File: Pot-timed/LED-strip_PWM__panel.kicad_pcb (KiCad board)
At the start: 2 copper layers, 160 x 100 mm, 76 parts, among them IC1 ATTINY13A-MM, P1 CONN_2, P2 CONN_2, T1 AO3400, U1 MCP1804-SOT23-5

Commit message: Pot-timed: Tweaked the panel (paste layer for stencil).
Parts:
- removed the 1PIN at (104.0, 97.0)
- removed the 1PIN at (256.0, 97.0)
- removed the 1PIN at (104.0, 92.0)
- added BH1: BH1, 1pin, F.Cu at (104.0, 97.0)
- added C1: 100nF, MADW__C0805, F.Cu at (198.4, 93.9)
- added C1: 100nF, MADW__C0805, F.Cu at (220.4, 93.9)
- added C1: 100nF, MADW__C0805, F.Cu at (220.4, 124.5)
- added C1: 100nF, MADW__C0805, F.Cu at (220.4, 155.2)
- added C1: 100nF, MADW__C0805, F.Cu at (209.4, 155.2)
- added C1: 100nF, MADW__C0805, F.Cu at (209.4, 124.5)
- added C1: 100nF, MADW__C0805, F.Cu at (209.4, 93.9)
- added C1: 100nF, MADW__C0805, F.Cu at (154.4, 93.9)
- added C1: 100nF, MADW__C0805, F.Cu at (154.4, 124.5)
- added C1: 100nF, MADW__C0805, F.Cu at (154.4, 155.2)
- added C1: 100nF, MADW__C0805, F.Cu at (165.4, 155.2)
- added C1: 100nF, MADW__C0805, F.Cu at (198.4, 124.5)
- added C1: 100nF, MADW__C0805, F.Cu at (165.4, 124.5)
- added C1: 100nF, MADW__C0805, F.Cu at (165.4, 93.9)
- added C1: 100nF, MADW__C0805, F.Cu at (187.4, 93.9)
- added C1: 100nF, MADW__C0805, F.Cu at (187.4, 124.5)
- added C1: 100nF, MADW__C0805, F.Cu at (187.4, 155.2)
- added C1: 100nF, MADW__C0805, F.Cu at (176.4, 155.2)
- added C1: 100nF, MADW__C0805, F.Cu at (176.4, 124.5)
- added C1: 100nF, MADW__C0805, F.Cu at (176.4, 93.9)
- added C1: 100nF, MADW__C0805, F.Cu at (132.4, 93.9)
- added C1: 100nF, MADW__C0805, F.Cu at (132.4, 124.5)
- added C1: 100nF, MADW__C0805, F.Cu at (198.4, 155.2)
- added C1: 100nF, MADW__C0805, F.Cu at (132.4, 155.2)
- added C1: 100nF, MADW__C0805, F.Cu at (143.4, 155.2)
- added C1: 100nF, MADW__C0805, F.Cu at (143.4, 124.5)
- added C1: 100nF, MADW__C0805, F.Cu at (143.4, 93.9)
- added C1: 100nF, MADW__C0805, F.Cu at (121.5, 93.9)
- added C1: 100nF, MADW__C0805, F.Cu at (121.5, 124.5)
- added C1: 100nF, MADW__C0805, F.Cu at (121.5, 155.2)
- added C1: 100nF, MADW__C0805, F.Cu at (231.4, 93.9)
- added C1: 100nF, MADW__C0805, F.Cu at (231.4, 124.5)
- added C1: 100nF, MADW__C0805, F.Cu at (231.4, 155.2)
- added C1: 100nF, MADW__C0805, F.Cu at (242.4, 155.2)
- added C1: 100nF, MADW__C0805, F.Cu at (242.4, 124.5)
- added C1: 100nF, MADW__C0805, F.Cu at (242.4, 93.9)
- added C2: 100nF, MADW__C0805, F.Cu at (204.4, 91.4)
- added C2: 100nF, MADW__C0805, F.Cu at (226.4, 91.4)
- added C2: 100nF, MADW__C0805, F.Cu at (226.4, 122.0)
- added C2: 100nF, MADW__C0805, F.Cu at (226.4, 152.7)
- added C2: 100nF, MADW__C0805, F.Cu at (215.4, 152.7)
- added C2: 100nF, MADW__C0805, F.Cu at (215.4, 122.0)
- added C2: 100nF, MADW__C0805, F.Cu at (215.4, 91.4)
- added C2: 100nF, MADW__C0805, F.Cu at (160.4, 91.4)
- added C2: 100nF, MADW__C0805, F.Cu at (160.4, 122.0)
- added C2: 100nF, MADW__C0805, F.Cu at (160.4, 152.7)
- added C2: 100nF, MADW__C0805, F.Cu at (171.4, 152.7)
- added C2: 100nF, MADW__C0805, F.Cu at (204.4, 122.0)
- added C2: 100nF, MADW__C0805, F.Cu at (171.4, 122.0)
- added C2: 100nF, MADW__C0805, F.Cu at (171.4, 91.4)
- added C2: 100nF, MADW__C0805, F.Cu at (193.4, 91.4)
- added C2: 100nF, MADW__C0805, F.Cu at (193.4, 122.0)
- added C2: 100nF, MADW__C0805, F.Cu at (193.4, 152.7)
- added C2: 100nF, MADW__C0805, F.Cu at (182.4, 152.7)
- added C2: 100nF, MADW__C0805, F.Cu at (182.4, 122.0)
- added C2: 100nF, MADW__C0805, F.Cu at (182.4, 91.4)
- added C2: 100nF, MADW__C0805, F.Cu at (138.4, 91.4)
- added C2: 100nF, MADW__C0805, F.Cu at (138.4, 122.0)
- added C2: 100nF, MADW__C0805, F.Cu at (204.4, 152.7)
- added C2: 100nF, MADW__C0805, F.Cu at (138.4, 152.7)
- added C2: 100nF, MADW__C0805, F.Cu at (149.4, 152.7)
- added C2: 100nF, MADW__C0805, F.Cu at (149.4, 122.0)
- added C2: 100nF, MADW__C0805, F.Cu at (149.4, 91.4)
- added C2: 100nF, MADW__C0805, F.Cu at (127.5, 91.4)
- added C2: 100nF, MADW__C0805, F.Cu at (127.5, 122.0)
- added C2: 100nF, MADW__C0805, F.Cu at (127.5, 152.7)
- added C2: 100nF, MADW__C0805, F.Cu at (237.4, 91.4)
- added C2: 100nF, MADW__C0805, F.Cu at (237.4, 122.0)
- added C2: 100nF, MADW__C0805, F.Cu at (237.4, 152.7)
- added C2: 100nF, MADW__C0805, F.Cu at (248.4, 152.7)
- added C2: 100nF, MADW__C0805, F.Cu at (248.4, 122.0)
- added C2: 100nF, MADW__C0805, F.Cu at (248.4, 91.4)
- added C3: 4.7µF, MADW__C0805, F.Cu at (200.9, 93.9)
- added C3: 4.7µF, MADW__C0805, F.Cu at (222.9, 93.9)
- added C3: 4.7µF, MADW__C0805, F.Cu at (222.9, 124.5)
- added C3: 4.7µF, MADW__C0805, F.Cu at (222.9, 155.2)
- added C3: 4.7µF, MADW__C0805, F.Cu at (211.9, 155.2)
- added C3: 4.7µF, MADW__C0805, F.Cu at (211.9, 124.5)
- added C3: 4.7µF, MADW__C0805, F.Cu at (211.9, 93.9)
- added C3: 4.7µF, MADW__C0805, F.Cu at (156.9, 93.9)
- added C3: 4.7µF, MADW__C0805, F.Cu at (156.9, 124.5)
- added C3: 4.7µF, MADW__C0805, F.Cu at (156.9, 155.2)
- added C3: 4.7µF, MADW__C0805, F.Cu at (167.9, 155.2)
- added C3: 4.7µF, MADW__C0805, F.Cu at (200.9, 124.5)
- added C3: 4.7µF, MADW__C0805, F.Cu at (167.9, 124.5)
- added C3: 4.7µF, MADW__C0805, F.Cu at (167.9, 93.9)
- added C3: 4.7µF, MADW__C0805, F.Cu at (189.9, 93.9)
- added C3: 4.7µF, MADW__C0805, F.Cu at (189.9, 124.5)
- added C3: 4.7µF, MADW__C0805, F.Cu at (189.9, 155.2)
- added C3: 4.7µF, MADW__C0805, F.Cu at (178.9, 155.2)
- added C3: 4.7µF, MADW__C0805, F.Cu at (178.9, 124.5)
- added C3: 4.7µF, MADW__C0805, F.Cu at (178.9, 93.9)
- added C3: 4.7µF, MADW__C0805, F.Cu at (134.9, 93.9)
- added C3: 4.7µF, MADW__C0805, F.Cu at (134.9, 124.5)
- added C3: 4.7µF, MADW__C0805, F.Cu at (200.9, 155.2)
- added C3: 4.7µF, MADW__C0805, F.Cu at (134.9, 155.2)
- added C3: 4.7µF, MADW__C0805, F.Cu at (145.9, 155.2)
- added C3: 4.7µF, MADW__C0805, F.Cu at (145.9, 124.5)
- added C3: 4.7µF, MADW__C0805, F.Cu at (145.9, 93.9)
- added C3: 4.7µF, MADW__C0805, F.Cu at (124.0, 93.9)
- added C3: 4.7µF, MADW__C0805, F.Cu at (124.0, 124.5)
- added C3: 4.7µF, MADW__C0805, F.Cu at (124.0, 155.2)
- added C3: 4.7µF, MADW__C0805, F.Cu at (233.9, 93.9)
- added C3: 4.7µF, MADW__C0805, F.Cu at (233.9, 124.5)
- added C3: 4.7µF, MADW__C0805, F.Cu at (233.9, 155.2)
- added C3: 4.7µF, MADW__C0805, F.Cu at (244.9, 155.2)
- added C3: 4.7µF, MADW__C0805, F.Cu at (244.9, 124.5)
- added C3: 4.7µF, MADW__C0805, F.Cu at (244.9, 93.9)
- added G1: OSHW-logo_silkscreen_3mm, OSHW-logo_silkscreen_3mm, B.Cu at (201.2, 105.5)
- added G1: OSHW-logo_silkscreen_3mm, OSHW-logo_silkscreen_3mm, B.Cu at (223.2, 105.5)
- added G1: OSHW-logo_silkscreen_3mm, OSHW-logo_silkscreen_3mm, B.Cu at (223.2, 136.1)
- added G1: OSHW-logo_silkscreen_3mm, OSHW-logo_silkscreen_3mm, B.Cu at (223.2, 166.8)
- added G1: OSHW-logo_silkscreen_3mm, OSHW-logo_silkscreen_3mm, B.Cu at (212.2, 166.8)
- added G1: OSHW-logo_silkscreen_3mm, OSHW-logo_silkscreen_3mm, B.Cu at (212.2, 136.1)
- added G1: OSHW-logo_silkscreen_3mm, OSHW-logo_silkscreen_3mm, B.Cu at (212.2, 105.5)
- added G1: OSHW-logo_silkscreen_3mm, OSHW-logo_silkscreen_3mm, B.Cu at (157.2, 105.5)
- added G1: OSHW-logo_silkscreen_3mm, OSHW-logo_silkscreen_3mm, B.Cu at (157.2, 136.1)
- added G1: OSHW-logo_silkscreen_3mm, OSHW-logo_silkscreen_3mm, B.Cu at (157.2, 166.8)
- added G1: OSHW-logo_silkscreen_3mm, OSHW-logo_silkscreen_3mm, B.Cu at (168.2, 166.8)
- added G1: OSHW-logo_silkscreen_3mm, OSHW-logo_silkscreen_3mm, B.Cu at (201.2, 136.1)
- added G1: OSHW-logo_silkscreen_3mm, OSHW-logo_silkscreen_3mm, B.Cu at (168.2, 136.1)
- added G1: OSHW-logo_silkscreen_3mm, OSHW-logo_silkscreen_3mm, B.Cu at (168.2, 105.5)
- added G1: OSHW-logo_silkscreen_3mm, OSHW-logo_silkscreen_3mm, B.Cu at (190.2, 105.5)
- added G1: OSHW-logo_silkscreen_3mm, OSHW-logo_silkscreen_3mm, B.Cu at (190.2, 136.1)
- added G1: OSHW-logo_silkscreen_3mm, OSHW-logo_silkscreen_3mm, B.Cu at (190.2, 166.8)
- added G1: OSHW-logo_silkscreen_3mm, OSHW-logo_silkscreen_3mm, B.Cu at (179.2, 166.8)
- added G1: OSHW-logo_silkscreen_3mm, OSHW-logo_silkscreen_3mm, B.Cu at (179.2, 136.1)
- added G1: OSHW-logo_silkscreen_3mm, OSHW-logo_silkscreen_3mm, B.Cu at (179.2, 105.5)
- added G1: OSHW-logo_silkscreen_3mm, OSHW-logo_silkscreen_3mm, B.Cu at (135.2, 105.5)
- added G1: OSHW-logo_silkscreen_3mm, OSHW-logo_silkscreen_3mm, B.Cu at (135.2, 136.1)
- added G1: OSHW-logo_silkscreen_3mm, OSHW-logo_silkscreen_3mm, B.Cu at (201.2, 166.8)
- added G1: OSHW-logo_silkscreen_3mm, OSHW-logo_silkscreen_3mm, B.Cu at (135.2, 166.8)
- added G1: OSHW-logo_silkscreen_3mm, OSHW-logo_silkscreen_3mm, B.Cu at (146.2, 166.8)
- added G1: OSHW-logo_silkscreen_3mm, OSHW-logo_silkscreen_3mm, B.Cu at (146.2, 136.1)
- added G1: OSHW-logo_silkscreen_3mm, OSHW-logo_silkscreen_3mm, B.Cu at (146.2, 105.5)
- added G1: OSHW-logo_silkscreen_3mm, OSHW-logo_silkscreen_3mm, B.Cu at (124.2, 105.5)
- added G1: OSHW-logo_silkscreen_3mm, OSHW-logo_silkscreen_3mm, B.Cu at (124.2, 136.1)
- added G1: OSHW-logo_silkscreen_3mm, OSHW-logo_silkscreen_3mm, B.Cu at (124.2, 166.8)
- added G1: OSHW-logo_silkscreen_3mm, OSHW-logo_silkscreen_3mm, B.Cu at (234.2, 105.5)
- added G1: OSHW-logo_silkscreen_3mm, OSHW-logo_silkscreen_3mm, B.Cu at (234.2, 136.1)
- added G1: OSHW-logo_silkscreen_3mm, OSHW-logo_silkscreen_3mm, B.Cu at (234.2, 166.8)
- added G1: OSHW-logo_silkscreen_3mm, OSHW-logo_silkscreen_3mm, B.Cu at (245.2, 166.8)
- added G1: OSHW-logo_silkscreen_3mm, OSHW-logo_silkscreen_3mm, B.Cu at (245.2, 136.1)
- added G1: OSHW-logo_silkscreen_3mm, OSHW-logo_silkscreen_3mm, B.Cu at (245.2, 105.5)
- added G2: LED_smile_silkscreen_3mm, LED_smile_silkscreen_3mm, B.Cu at (201.2, 93.4)
- added G2: LED_smile_silkscreen_3mm, LED_smile_silkscreen_3mm, B.Cu at (223.2, 93.4)
- added G2: LED_smile_silkscreen_3mm, LED_smile_silkscreen_3mm, B.Cu at (223.2, 124.1)
- added G2: LED_smile_silkscreen_3mm, LED_smile_silkscreen_3mm, B.Cu at (223.2, 154.7)
- added G2: LED_smile_silkscreen_3mm, LED_smile_silkscreen_3mm, B.Cu at (212.2, 154.7)
- added G2: LED_smile_silkscreen_3mm, LED_smile_silkscreen_3mm, B.Cu at (212.2, 124.1)
- added G2: LED_smile_silkscreen_3mm, LED_smile_silkscreen_3mm, B.Cu at (212.2, 93.4)
- added G2: LED_smile_silkscreen_3mm, LED_smile_silkscreen_3mm, B.Cu at (157.2, 93.4)
- added G2: LED_smile_silkscreen_3mm, LED_smile_silkscreen_3mm, B.Cu at (157.2, 124.1)
- added G2: LED_smile_silkscreen_3mm, LED_smile_silkscreen_3mm, B.Cu at (157.2, 154.7)
- added G2: LED_smile_silkscreen_3mm, LED_smile_silkscreen_3mm, B.Cu at (168.2, 154.7)
- added G2: LED_smile_silkscreen_3mm, LED_smile_silkscreen_3mm, B.Cu at (201.2, 124.1)
- added G2: LED_smile_silkscreen_3mm, LED_smile_silkscreen_3mm, B.Cu at (168.2, 124.1)
- added G2: LED_smile_silkscreen_3mm, LED_smile_silkscreen_3mm, B.Cu at (168.2, 93.4)
- added G2: LED_smile_silkscreen_3mm, LED_smile_silkscreen_3mm, B.Cu at (190.2, 93.4)
- added G2: LED_smile_silkscreen_3mm, LED_smile_silkscreen_3mm, B.Cu at (190.2, 124.1)
- added G2: LED_smile_silkscreen_3mm, LED_smile_silkscreen_3mm, B.Cu at (190.2, 154.7)
- added G2: LED_smile_silkscreen_3mm, LED_smile_silkscreen_3mm, B.Cu at (179.2, 154.7)
- added G2: LED_smile_silkscreen_3mm, LED_smile_silkscreen_3mm, B.Cu at (179.2, 124.1)
- added G2: LED_smile_silkscreen_3mm, LED_smile_silkscreen_3mm, B.Cu at (179.2, 93.4)
- added G2: LED_smile_silkscreen_3mm, LED_smile_silkscreen_3mm, B.Cu at (135.2, 93.4)
- added G2: LED_smile_silkscreen_3mm, LED_smile_silkscreen_3mm, B.Cu at (135.2, 124.1)
- added G2: LED_smile_silkscreen_3mm, LED_smile_silkscreen_3mm, B.Cu at (201.2, 154.7)
- added G2: LED_smile_silkscreen_3mm, LED_smile_silkscreen_3mm, B.Cu at (135.2, 154.7)
- added G2: LED_smile_silkscreen_3mm, LED_smile_silkscreen_3mm, B.Cu at (146.2, 154.7)
- added G2: LED_smile_silkscreen_3mm, LED_smile_silkscreen_3mm, B.Cu at (146.2, 124.1)
- added G2: LED_smile_silkscreen_3mm, LED_smile_silkscreen_3mm, B.Cu at (146.2, 93.4)
- added G2: LED_smile_silkscreen_3mm, LED_smile_silkscreen_3mm, B.Cu at (124.2, 93.4)
- added G2: LED_smile_silkscreen_3mm, LED_smile_silkscreen_3mm, B.Cu at (124.2, 124.1)
- added G2: LED_smile_silkscreen_3mm, LED_smile_silkscreen_3mm, B.Cu at (124.2, 154.7)
- added G2: LED_smile_silkscreen_3mm, LED_smile_silkscreen_3mm, B.Cu at (234.2, 93.4)
- added G2: LED_smile_silkscreen_3mm, LED_smile_silkscreen_3mm, B.Cu at (234.2, 124.1)
- added G2: LED_smile_silkscreen_3mm, LED_smile_silkscreen_3mm, B.Cu at (234.2, 154.7)
- added G2: LED_smile_silkscreen_3mm, LED_smile_silkscreen_3mm, B.Cu at (245.2, 154.7)
- added G2: LED_smile_silkscreen_3mm, LED_smile_silkscreen_3mm, B.Cu at (245.2, 124.1)
- added G2: LED_smile_silkscreen_3mm, LED_smile_silkscreen_3mm, B.Cu at (245.2, 93.4)
- added IC1: ATTINY13A-MM, MADW__MLF10, F.Cu at (204.2, 99.2)
- added IC1: ATTINY13A-MM, MADW__MLF10, F.Cu at (226.2, 99.2)
- added IC1: ATTINY13A-MM, MADW__MLF10, F.Cu at (226.2, 129.9)
- added IC1: ATTINY13A-MM, MADW__MLF10, F.Cu at (226.2, 160.5)
- added IC1: ATTINY13A-MM, MADW__MLF10, F.Cu at (215.2, 160.5)
- added IC1: ATTINY13A-MM, MADW__MLF10, F.Cu at (215.2, 129.9)
- added IC1: ATTINY13A-MM, MADW__MLF10, F.Cu at (215.2, 99.2)
- added IC1: ATTINY13A-MM, MADW__MLF10, F.Cu at (160.2, 99.2)
- added IC1: ATTINY13A-MM, MADW__MLF10, F.Cu at (160.2, 129.9)
- added IC1: ATTINY13A-MM, MADW__MLF10, F.Cu at (160.2, 160.5)
- added IC1: ATTINY13A-MM, MADW__MLF10, F.Cu at (171.2, 160.5)
- added IC1: ATTINY13A-MM, MADW__MLF10, F.Cu at (204.2, 129.9)
- added IC1: ATTINY13A-MM, MADW__MLF10, F.Cu at (171.2, 129.9)
- added IC1: ATTINY13A-MM, MADW__MLF10, F.Cu at (171.2, 99.2)
- added IC1: ATTINY13A-MM, MADW__MLF10, F.Cu at (193.2, 99.2)
- added IC1: ATTINY13A-MM, MADW__MLF10, F.Cu at (193.2, 129.9)
- added IC1: ATTINY13A-MM, MADW__MLF10, F.Cu at (193.2, 160.5)
- added IC1: ATTINY13A-MM, MADW__MLF10, F.Cu at (182.2, 160.5)
- added IC1: ATTINY13A-MM, MADW__MLF10, F.Cu at (182.2, 129.9)
- added IC1: ATTINY13A-MM, MADW__MLF10, F.Cu at (182.2, 99.2)
- added IC1: ATTINY13A-MM, MADW__MLF10, F.Cu at (138.2, 99.2)
- added IC1: ATTINY13A-MM, MADW__MLF10, F.Cu at (138.2, 129.9)
- added IC1: ATTINY13A-MM, MADW__MLF10, F.Cu at (204.2, 160.5)
- added IC1: ATTINY13A-MM, MADW__MLF10, F.Cu at (138.2, 160.5)
- added IC1: ATTINY13A-MM, MADW__MLF10, F.Cu at (149.2, 160.5)
- added IC1: ATTINY13A-MM, MADW__MLF10, F.Cu at (149.2, 129.9)
- added IC1: ATTINY13A-MM, MADW__MLF10, F.Cu at (149.2, 99.2)
- added IC1: ATTINY13A-MM, MADW__MLF10, F.Cu at (127.2, 99.2)
- added IC1: ATTINY13A-MM, MADW__MLF10, F.Cu at (127.2, 129.9)
- added IC1: ATTINY13A-MM, MADW__MLF10, F.Cu at (127.2, 160.5)
- added IC1: ATTINY13A-MM, MADW__MLF10, F.Cu at (237.2, 99.2)
- added IC1: ATTINY13A-MM, MADW__MLF10, F.Cu at (237.2, 129.9)
- added IC1: ATTINY13A-MM, MADW__MLF10, F.Cu at (237.2, 160.5)
- added IC1: ATTINY13A-MM, MADW__MLF10, F.Cu at (248.2, 160.5)
- added IC1: ATTINY13A-MM, MADW__MLF10, F.Cu at (248.2, 129.9)
- added IC1: ATTINY13A-MM, MADW__MLF10, F.Cu at (248.2, 99.2)
- added JP1: ISP, MADW__PIN_ARRAY_3x2_1.27mm, F.Cu at (199.7, 99.2)
- added JP1: ISP, MADW__PIN_ARRAY_3x2_1.27mm, F.Cu at (221.7, 99.2)
- added JP1: ISP, MADW__PIN_ARRAY_3x2_1.27mm, F.Cu at (221.7, 129.9)
- added JP1: ISP, MADW__PIN_ARRAY_3x2_1.27mm, F.Cu at (221.7, 160.5)
- added JP1: ISP, MADW__PIN_ARRAY_3x2_1.27mm, F.Cu at (210.7, 160.5)
- added JP1: ISP, MADW__PIN_ARRAY_3x2_1.27mm, F.Cu at (210.7, 129.9)
- added JP1: ISP, MADW__PIN_ARRAY_3x2_1.27mm, F.Cu at (210.7, 99.2)
- added JP1: ISP, MADW__PIN_ARRAY_3x2_1.27mm, F.Cu at (155.7, 99.2)
- added JP1: ISP, MADW__PIN_ARRAY_3x2_1.27mm, F.Cu at (155.7, 129.9)
- added JP1: ISP, MADW__PIN_ARRAY_3x2_1.27mm, F.Cu at (155.7, 160.5)
- added JP1: ISP, MADW__PIN_ARRAY_3x2_1.27mm, F.Cu at (166.7, 160.5)
- added JP1: ISP, MADW__PIN_ARRAY_3x2_1.27mm, F.Cu at (199.7, 129.9)
- added JP1: ISP, MADW__PIN_ARRAY_3x2_1.27mm, F.Cu at (166.7, 129.9)
- added JP1: ISP, MADW__PIN_ARRAY_3x2_1.27mm, F.Cu at (166.7, 99.2)
- added JP1: ISP, MADW__PIN_ARRAY_3x2_1.27mm, F.Cu at (188.7, 99.2)
- added JP1: ISP, MADW__PIN_ARRAY_3x2_1.27mm, F.Cu at (188.7, 129.9)
- added JP1: ISP, MADW__PIN_ARRAY_3x2_1.27mm, F.Cu at (188.7, 160.5)
- added JP1: ISP, MADW__PIN_ARRAY_3x2_1.27mm, F.Cu at (177.7, 160.5)
- added JP1: ISP, MADW__PIN_ARRAY_3x2_1.27mm, F.Cu at (177.7, 129.9)
- added JP1: ISP, MADW__PIN_ARRAY_3x2_1.27mm, F.Cu at (177.7, 99.2)
- added JP1: ISP, MADW__PIN_ARRAY_3x2_1.27mm, F.Cu at (133.7, 99.2)
- added JP1: ISP, MADW__PIN_ARRAY_3x2_1.27mm, F.Cu at (133.7, 129.9)
- added JP1: ISP, MADW__PIN_ARRAY_3x2_1.27mm, F.Cu at (199.7, 160.5)
- added JP1: ISP, MADW__PIN_ARRAY_3x2_1.27mm, F.Cu at (133.7, 160.5)
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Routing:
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
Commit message: Pot-timed: Panel partially updated.
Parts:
- removed the C1 at (198.4, 93.9)
- removed the C1 at (220.4, 93.9)
- removed the C1 at (220.4, 124.5)
- removed the C1 at (220.4, 155.2)
- removed the C1 at (209.4, 155.2)
- removed the C1 at (209.4, 124.5)
- removed the C1 at (209.4, 93.9)
- removed the C1 at (154.4, 93.9)
- removed the C1 at (154.4, 124.5)
- removed the C1 at (154.4, 155.2)
- removed the C1 at (165.4, 155.2)
- removed the C1 at (198.4, 124.5)
- removed the C1 at (165.4, 124.5)
- removed the C1 at (165.4, 93.9)
- removed the C1 at (187.4, 93.9)
- removed the C1 at (187.4, 124.5)
- removed the C1 at (187.4, 155.2)
- removed the C1 at (176.4, 155.2)
- removed the C1 at (176.4, 124.5)
- removed the C1 at (176.4, 93.9)
- removed the C1 at (132.4, 93.9)
- removed the C1 at (132.4, 124.5)
- removed the C1 at (198.4, 155.2)
- removed the C1 at (132.4, 155.2)
- removed the C1 at (143.4, 155.2)
- removed the C1 at (143.4, 124.5)
- removed the C1 at (143.4, 93.9)
- removed the C1 at (121.5, 93.9)
- removed the C1 at (121.5, 124.5)
- removed the C1 at (121.5, 155.2)
- removed the C1 at (231.4, 93.9)
- removed the C1 at (231.4, 124.5)
- removed the C1 at (231.4, 155.2)
- removed the C1 at (242.4, 155.2)
- removed the C1 at (242.4, 124.5)
- removed the C1 at (242.4, 93.9)
- removed the C2 at (204.4, 91.4)
- removed the C2 at (226.4, 91.4)
- removed the C2 at (226.4, 122.0)
- removed the C2 at (226.4, 152.7)
- removed the C2 at (215.4, 152.7)
- removed the C2 at (215.4, 122.0)
- removed the C2 at (215.4, 91.4)
- removed the C2 at (160.4, 91.4)
- removed the C2 at (160.4, 122.0)
- removed the C2 at (160.4, 152.7)
- removed the C2 at (171.4, 152.7)
- removed the C2 at (204.4, 122.0)
- removed the C2 at (171.4, 122.0)
- removed the C2 at (171.4, 91.4)
- removed the C2 at (193.4, 91.4)
- removed the C2 at (193.4, 122.0)
- removed the C2 at (193.4, 152.7)
- removed the C2 at (182.4, 152.7)
- removed the C2 at (182.4, 122.0)
- removed the C2 at (182.4, 91.4)
- removed the C2 at (138.4, 91.4)
- removed the C2 at (138.4, 122.0)
- removed the C2 at (204.4, 152.7)
- removed the C2 at (138.4, 152.7)
- removed the C2 at (149.4, 152.7)
- removed the C2 at (149.4, 122.0)
- removed the C2 at (149.4, 91.4)
- removed the C2 at (127.5, 91.4)
- removed the C2 at (127.5, 122.0)
- removed the C2 at (127.5, 152.7)
- removed the C2 at (237.4, 91.4)
- removed the C2 at (237.4, 122.0)
- removed the C2 at (237.4, 152.7)
- removed the C2 at (248.4, 152.7)
- removed the C2 at (248.4, 122.0)
- removed the C2 at (248.4, 91.4)
- removed the C3 at (200.9, 93.9)
- removed the C3 at (222.9, 93.9)
- removed the C3 at (222.9, 124.5)
- removed the C3 at (222.9, 155.2)
- removed the C3 at (211.9, 155.2)
- removed the C3 at (211.9, 124.5)
- removed the C3 at (211.9, 93.9)
- removed the C3 at (156.9, 93.9)
- removed the C3 at (156.9, 124.5)
- removed the C3 at (156.9, 155.2)
- removed the C3 at (167.9, 155.2)
- removed the C3 at (200.9, 124.5)
- removed the C3 at (167.9, 124.5)
- removed the C3 at (167.9, 93.9)
- removed the C3 at (189.9, 93.9)
- removed the C3 at (189.9, 124.5)
- removed the C3 at (189.9, 155.2)
- removed the C3 at (178.9, 155.2)
- removed the C3 at (178.9, 124.5)
- removed the C3 at (178.9, 93.9)
- removed the C3 at (134.9, 93.9)
- removed the C3 at (134.9, 124.5)
- removed the C3 at (200.9, 155.2)
- removed the C3 at (134.9, 155.2)
- removed the C3 at (145.9, 155.2)
- removed the C3 at (145.9, 124.5)
- removed the C3 at (145.9, 93.9)
- removed the C3 at (124.0, 93.9)
- removed the C3 at (124.0, 124.5)
- removed the C3 at (124.0, 155.2)
- removed the C3 at (233.9, 93.9)
- removed the C3 at (233.9, 124.5)
- removed the C3 at (233.9, 155.2)
- removed the C3 at (244.9, 155.2)
- removed the C3 at (244.9, 124.5)
- removed the C3 at (244.9, 93.9)
- removed the G1 at (201.2, 105.5)
- removed the G1 at (223.2, 105.5)
- removed the G1 at (223.2, 136.1)
- removed the G1 at (223.2, 166.8)
- removed the G1 at (212.2, 166.8)
- removed the G1 at (212.2, 136.1)
- removed the G1 at (212.2, 105.5)
- removed the G1 at (157.2, 105.5)
- removed the G1 at (157.2, 136.1)
- removed the G1 at (157.2, 166.8)
- removed the G1 at (168.2, 166.8)
- removed the G1 at (201.2, 136.1)
- removed the G1 at (168.2, 136.1)
- removed the G1 at (168.2, 105.5)
- removed the G1 at (190.2, 105.5)
- removed the G1 at (190.2, 136.1)
- removed the G1 at (190.2, 166.8)
- removed the G1 at (179.2, 166.8)
- removed the G1 at (179.2, 136.1)
- removed the G1 at (179.2, 105.5)
- removed the G1 at (135.2, 105.5)
- removed the G1 at (135.2, 136.1)
- removed the G1 at (201.2, 166.8)
- removed the G1 at (135.2, 166.8)
- removed the G1 at (146.2, 166.8)
- removed the G1 at (146.2, 136.1)
- removed the G1 at (146.2, 105.5)
- removed the G1 at (124.2, 105.5)
- removed the G1 at (124.2, 136.1)
- removed the G1 at (124.2, 166.8)
- removed the G1 at (113.2, 166.8)
- removed the G1 at (113.2, 136.1)
- removed the G1 at (113.2, 105.5)
- removed the G1 at (234.2, 105.5)
- removed the G1 at (234.2, 136.1)
- removed the G1 at (234.2, 166.8)
- removed the G1 at (245.2, 166.8)
- removed the G1 at (245.2, 136.1)
- removed the G1 at (245.2, 105.5)
- removed the G2 at (201.2, 93.4)
- removed the G2 at (223.2, 93.4)
- removed the G2 at (223.2, 124.1)
- removed the G2 at (223.2, 154.7)
- removed the G2 at (212.2, 154.7)
- removed the G2 at (212.2, 124.1)
- removed the G2 at (212.2, 93.4)
- removed the G2 at (157.2, 93.4)
- removed the G2 at (157.2, 124.1)
- removed the G2 at (157.2, 154.7)
- removed the G2 at (168.2, 154.7)
- removed the G2 at (201.2, 124.1)
- removed the G2 at (168.2, 124.1)
- removed the G2 at (168.2, 93.4)
- removed the G2 at (190.2, 93.4)
- removed the G2 at (190.2, 124.1)
- removed the G2 at (190.2, 154.7)
- removed the G2 at (179.2, 154.7)
- removed the G2 at (179.2, 124.1)
- removed the G2 at (179.2, 93.4)
- removed the G2 at (135.2, 93.4)
- removed the G2 at (135.2, 124.1)
- removed the G2 at (201.2, 154.7)
- removed the G2 at (135.2, 154.7)
- removed the G2 at (146.2, 154.7)
- removed the G2 at (146.2, 124.1)
- removed the G2 at (146.2, 93.4)
- removed the G2 at (124.2, 93.4)
- removed the G2 at (124.2, 124.1)
- removed the G2 at (124.2, 154.7)
- removed the G2 at (113.2, 154.7)
- removed the G2 at (113.2, 124.1)
- removed the G2 at (113.2, 93.4)
- removed the G2 at (234.2, 93.4)
- removed the G2 at (234.2, 124.1)
- removed the G2 at (234.2, 154.7)
- removed the G2 at (245.2, 154.7)
- removed the G2 at (245.2, 124.1)
- removed the G2 at (245.2, 93.4)
- removed the IC1 at (204.2, 99.2)
- removed the IC1 at (226.2, 99.2)
- removed the IC1 at (226.2, 129.9)
- removed the IC1 at (226.2, 160.5)
- removed the IC1 at (215.2, 160.5)
- removed the IC1 at (215.2, 129.9)
- removed the IC1 at (215.2, 99.2)
- removed the IC1 at (160.2, 99.2)
- removed the IC1 at (160.2, 129.9)
- removed the IC1 at (160.2, 160.5)
- removed the IC1 at (171.2, 160.5)
- removed the IC1 at (204.2, 129.9)
- removed the IC1 at (171.2, 129.9)
- removed the IC1 at (171.2, 99.2)
- removed the IC1 at (193.2, 99.2)
- removed the IC1 at (193.2, 129.9)
- removed the IC1 at (193.2, 160.5)
- removed the IC1 at (182.2, 160.5)
- removed the IC1 at (182.2, 129.9)
- removed the IC1 at (182.2, 99.2)
- removed the IC1 at (138.2, 99.2)
- removed the IC1 at (138.2, 129.9)
- removed the IC1 at (204.2, 160.5)
- removed the IC1 at (138.2, 160.5)
- removed the IC1 at (149.2, 160.5)
- removed the IC1 at (149.2, 129.9)
- removed the IC1 at (149.2, 99.2)
- removed the IC1 at (127.2, 99.2)
- removed the IC1 at (127.2, 129.9)
- removed the IC1 at (127.2, 160.5)
- removed the IC1 at (237.2, 99.2)
- removed the IC1 at (237.2, 129.9)
- removed the IC1 at (237.2, 160.5)
- removed the IC1 at (248.2, 160.5)
- removed the IC1 at (248.2, 129.9)
- removed the IC1 at (248.2, 99.2)
- removed the JP1 at (199.7, 99.2)
- removed the JP1 at (221.7, 99.2)
- removed the JP1 at (221.7, 129.9)
- removed the JP1 at (221.7, 160.5)
- removed the JP1 at (210.7, 160.5)
- removed the JP1 at (210.7, 129.9)
- removed the JP1 at (210.7, 99.2)
- removed the JP1 at (155.7, 99.2)
- removed the JP1 at (155.7, 129.9)
- removed the JP1 at (155.7, 160.5)
- removed the JP1 at (166.7, 160.5)
- removed the JP1 at (199.7, 129.9)
- removed the JP1 at (166.7, 129.9)
- removed the JP1 at (166.7, 99.2)
- removed the JP1 at (188.7, 99.2)
- removed the JP1 at (188.7, 129.9)
- removed the JP1 at (188.7, 160.5)
- removed the JP1 at (177.7, 160.5)
- removed the JP1 at (177.7, 129.9)
- removed the JP1 at (177.7, 99.2)
- removed the JP1 at (133.7, 99.2)
- removed the JP1 at (133.7, 129.9)
- removed the JP1 at (199.7, 160.5)
- removed the JP1 at (133.7, 160.5)
- removed the JP1 at (144.7, 160.5)
- removed the JP1 at (144.7, 129.9)
- removed the JP1 at (144.7, 99.2)
- removed the JP1 at (122.7, 99.2)
- removed the JP1 at (122.7, 129.9)
- removed the JP1 at (122.7, 160.5)
- removed the JP1 at (232.7, 99.2)
- removed the JP1 at (232.7, 129.9)
- removed the JP1 at (232.7, 160.5)
- removed the JP1 at (243.7, 160.5)
- removed the JP1 at (243.7, 129.9)
- removed the JP1 at (243.7, 99.2)
- removed the NJ1 at (200.9, 90.8)
- removed the NJ1 at (222.9, 90.8)
- removed the NJ1 at (222.9, 121.5)
- removed the NJ1 at (222.9, 152.1)
- removed the NJ1 at (211.9, 152.1)
- removed the NJ1 at (211.9, 121.5)
- removed the NJ1 at (211.9, 90.8)
- removed the NJ1 at (156.9, 90.8)
- removed the NJ1 at (156.9, 121.5)
- removed the NJ1 at (156.9, 152.1)
- removed the NJ1 at (167.9, 152.1)
- removed the NJ1 at (200.9, 121.5)
- removed the NJ1 at (167.9, 121.5)
- removed the NJ1 at (167.9, 90.8)
- removed the NJ1 at (189.9, 90.8)
- removed the NJ1 at (189.9, 121.5)
- removed the NJ1 at (189.9, 152.1)
- removed the NJ1 at (178.9, 152.1)
- removed the NJ1 at (178.9, 121.5)
- removed the NJ1 at (178.9, 90.8)
- removed the NJ1 at (134.9, 90.8)
- removed the NJ1 at (134.9, 121.5)
- removed the NJ1 at (200.9, 152.1)
- removed the NJ1 at (134.9, 152.1)
- removed the NJ1 at (145.9, 152.1)
- removed the NJ1 at (145.9, 121.5)
- removed the NJ1 at (145.9, 90.8)
- removed the NJ1 at (124.0, 90.8)
- removed the NJ1 at (124.0, 121.5)
- removed the NJ1 at (124.0, 152.1)
- removed the NJ1 at (233.9, 90.8)
- removed the NJ1 at (233.9, 121.5)
- removed the NJ1 at (233.9, 152.1)
- removed the NJ1 at (244.9, 152.1)
- removed the NJ1 at (244.9, 121.5)
- removed the NJ1 at (244.9, 90.8)
- removed the P1 at (202.0, 88.3)
- removed the P1 at (224.0, 88.3)
- removed the P1 at (224.0, 118.9)
- removed the P1 at (224.0, 149.6)
- removed the P1 at (213.0, 149.6)
- removed the P1 at (213.0, 118.9)
- removed the P1 at (213.0, 88.3)
- removed the P1 at (158.0, 88.3)
- removed the P1 at (158.0, 118.9)
- removed the P1 at (158.0, 149.6)
- removed the P1 at (169.0, 149.6)
- removed the P1 at (202.0, 118.9)
- removed the P1 at (169.0, 118.9)
- removed the P1 at (169.0, 88.3)
- removed the P1 at (191.0, 88.3)
- removed the P1 at (191.0, 118.9)
- removed the P1 at (191.0, 149.6)
- removed the P1 at (180.0, 149.6)
- removed the P1 at (180.0, 118.9)
- removed the P1 at (180.0, 88.3)
- removed the P1 at (136.0, 88.3)
- removed the P1 at (136.0, 118.9)
- removed the P1 at (202.0, 149.6)
- removed the P1 at (136.0, 149.6)
- removed the P1 at (147.0, 149.6)
- removed the P1 at (147.0, 118.9)
- removed the P1 at (147.0, 88.3)
- removed the P1 at (125.0, 88.3)
- removed the P1 at (125.0, 118.9)
- removed the P1 at (125.0, 149.6)
- removed the P1 at (235.0, 88.3)
- removed the P1 at (235.0, 118.9)
- removed the P1 at (235.0, 149.6)
- removed the P1 at (246.0, 149.6)
- removed the P1 at (246.0, 118.9)
- removed the P1 at (246.0, 88.3)
- removed the P2 at (202.0, 114.5)
- removed the P2 at (224.0, 114.5)
- removed the P2 at (224.0, 145.1)
- removed the P2 at (224.0, 175.8)
- removed the P2 at (213.0, 175.8)
- removed the P2 at (213.0, 145.1)
- removed the P2 at (213.0, 114.5)
- removed the P2 at (158.0, 114.5)
- removed the P2 at (158.0, 145.1)
- removed the P2 at (158.0, 175.8)
- removed the P2 at (169.0, 175.8)
- removed the P2 at (202.0, 145.1)
- removed the P2 at (169.0, 145.1)
- removed the P2 at (169.0, 114.5)
- removed the P2 at (191.0, 114.5)
- removed the P2 at (191.0, 145.1)
- removed the P2 at (191.0, 175.8)
- removed the P2 at (180.0, 175.8)
- removed the P2 at (180.0, 145.1)
- removed the P2 at (180.0, 114.5)
- removed the P2 at (136.0, 114.5)
- removed the P2 at (136.0, 145.1)
- removed the P2 at (202.0, 175.8)
- removed the P2 at (136.0, 175.8)
- removed the P2 at (147.0, 175.8)
- removed the P2 at (147.0, 145.1)
- removed the P2 at (147.0, 114.5)
- removed the P2 at (125.0, 114.5)
- removed the P2 at (125.0, 145.1)
- removed the P2 at (125.0, 175.8)
- removed the P2 at (235.0, 114.5)
- removed the P2 at (235.0, 145.1)
- removed the P2 at (235.0, 175.8)
- removed the P2 at (246.0, 175.8)
- removed the P2 at (246.0, 145.1)
- removed the P2 at (246.0, 114.5)
- removed the R1 at (198.8, 110.4)
- removed the R1 at (220.8, 110.4)
- removed the R1 at (220.8, 141.0)
- removed the R1 at (220.8, 171.7)
- removed the R1 at (209.8, 171.7)
- removed the R1 at (209.8, 141.0)
- removed the R1 at (209.8, 110.4)
- removed the R1 at (154.8, 110.4)
- removed the R1 at (154.8, 141.0)
- removed the R1 at (154.8, 171.7)
- removed the R1 at (165.8, 171.7)
- removed the R1 at (198.8, 141.0)
- removed the R1 at (165.8, 141.0)
- removed the R1 at (165.8, 110.4)
- removed the R1 at (187.8, 110.4)
- removed the R1 at (187.8, 141.0)
- removed the R1 at (187.8, 171.7)
- removed the R1 at (176.8, 171.7)
- removed the R1 at (176.8, 141.0)
- removed the R1 at (176.8, 110.4)
- removed the R1 at (132.8, 110.4)
- removed the R1 at (132.8, 141.0)
- removed the R1 at (198.8, 171.7)
- removed the R1 at (132.8, 171.7)
- removed the R1 at (143.8, 171.7)
- removed the R1 at (143.8, 141.0)
- removed the R1 at (143.8, 110.4)
- removed the R1 at (121.8, 110.4)
- removed the R1 at (121.8, 141.0)
- removed the R1 at (121.8, 171.7)
- removed the R1 at (231.8, 110.4)
- removed the R1 at (231.8, 141.0)
- removed the R1 at (231.8, 171.7)
- removed the R1 at (242.8, 171.7)
- removed the R1 at (242.8, 141.0)
- removed the R1 at (242.8, 110.4)
- removed the R2 at (205.2, 110.3)
- removed the R2 at (227.2, 110.3)
- removed the R2 at (227.2, 140.9)
- removed the R2 at (227.2, 171.6)
- removed the R2 at (216.2, 171.6)
- removed the R2 at (216.2, 140.9)
- removed the R2 at (216.2, 110.3)
- removed the R2 at (161.2, 110.3)
- removed the R2 at (161.2, 140.9)
- removed the R2 at (161.2, 171.6)
- removed the R2 at (172.2, 171.6)
- removed the R2 at (205.2, 140.9)
- removed the R2 at (172.2, 140.9)
- removed the R2 at (172.2, 110.3)
- removed the R2 at (194.2, 110.3)
- removed the R2 at (194.2, 140.9)
- removed the R2 at (194.2, 171.6)
- removed the R2 at (183.2, 171.6)
- removed the R2 at (183.2, 140.9)
- removed the R2 at (183.2, 110.3)
- removed the R2 at (139.2, 110.3)
- removed the R2 at (139.2, 140.9)
- removed the R2 at (205.2, 171.6)
- removed the R2 at (139.2, 171.6)
- removed the R2 at (150.2, 171.6)
- removed the R2 at (150.2, 140.9)
- removed the R2 at (150.2, 110.3)
- removed the R2 at (128.2, 110.3)
- removed the R2 at (128.2, 140.9)
- removed the R2 at (128.2, 171.6)
- removed the R2 at (238.2, 110.3)
- removed the R2 at (238.2, 140.9)
- removed the R2 at (238.2, 171.6)
- removed the R2 at (249.2, 171.6)
- removed the R2 at (249.2, 140.9)
- removed the R2 at (249.2, 110.3)
- removed the RV1 at (200.0, 105.0)
- removed the RV1 at (222.0, 105.0)
- removed the RV1 at (222.0, 135.6)
- removed the RV1 at (222.0, 166.3)
- removed the RV1 at (211.0, 166.3)
- removed the RV1 at (211.0, 135.6)
- removed the RV1 at (211.0, 105.0)
- removed the RV1 at (156.0, 105.0)
- removed the RV1 at (156.0, 135.6)
- removed the RV1 at (156.0, 166.3)
- removed the RV1 at (167.0, 166.3)
- removed the RV1 at (200.0, 135.6)
- removed the RV1 at (167.0, 135.6)
- removed the RV1 at (167.0, 105.0)
- removed the RV1 at (189.0, 105.0)
- removed the RV1 at (189.0, 135.6)
- removed the RV1 at (189.0, 166.3)
- removed the RV1 at (178.0, 166.3)
- removed the RV1 at (178.0, 135.6)
- removed the RV1 at (178.0, 105.0)
- removed the RV1 at (134.0, 105.0)
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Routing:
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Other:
- board text added: "12V"
- board text added: "LED"
- board text added: "V0.11 POT PWM controller"
- board text removed: "V0.10 POT PWM controller"

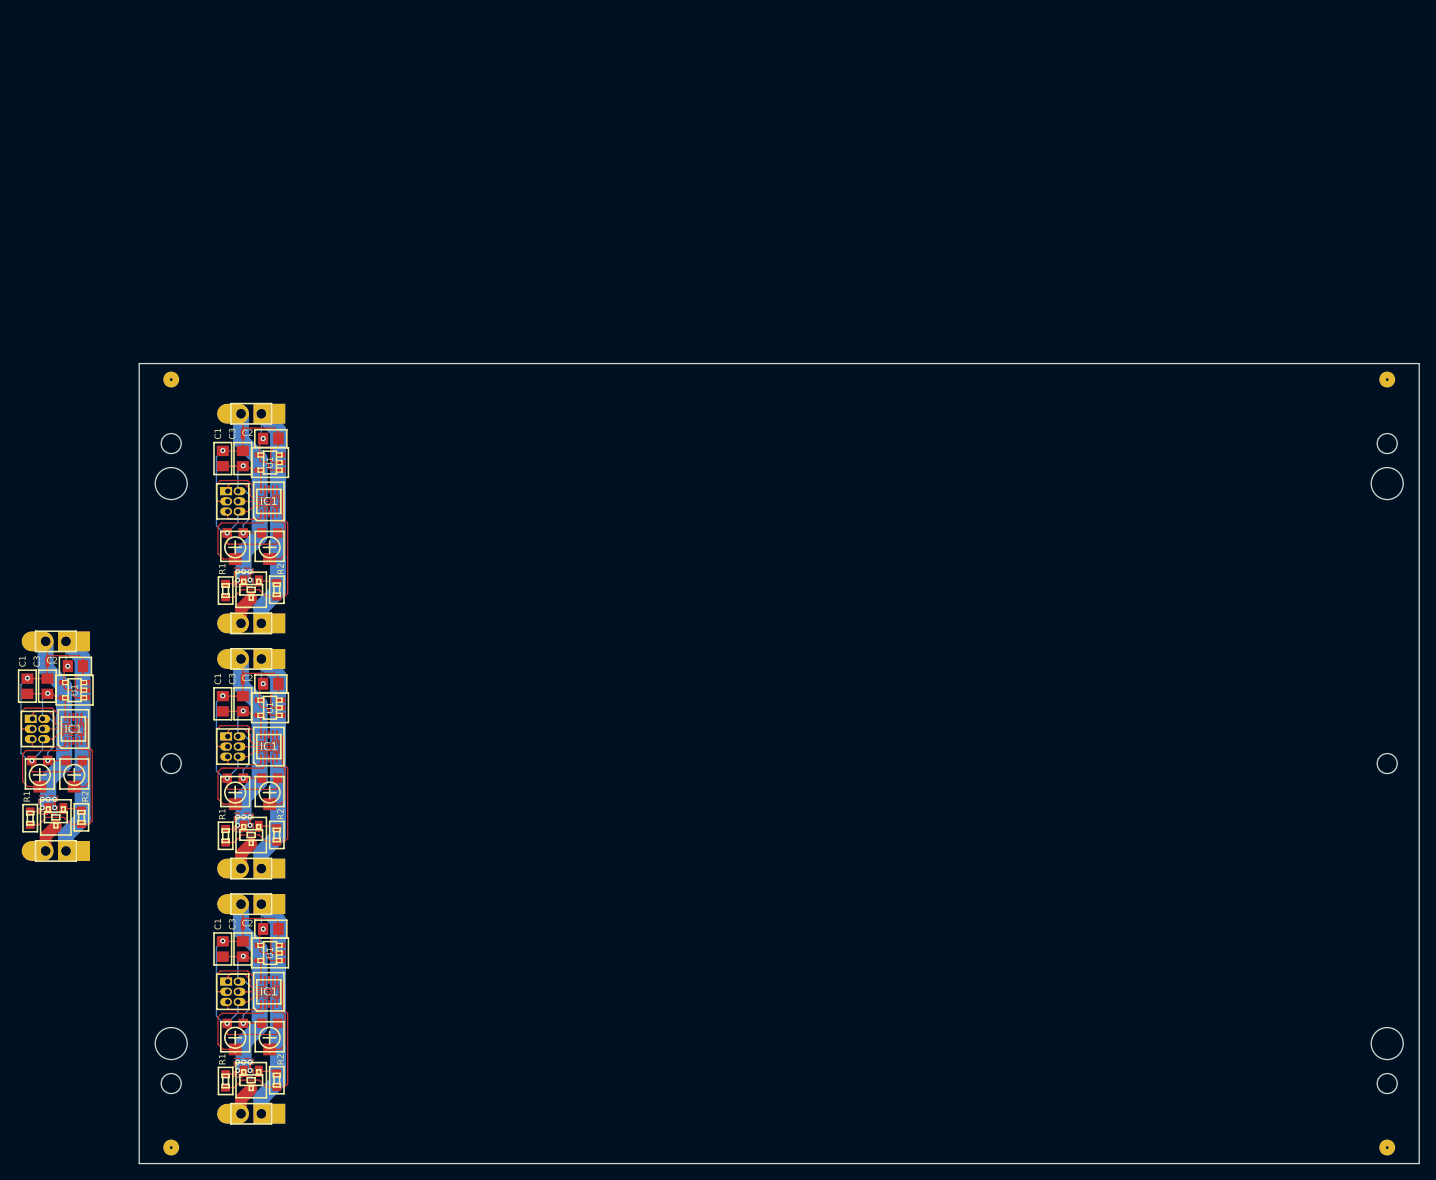
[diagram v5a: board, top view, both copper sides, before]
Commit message: Pot-timed (single board): tweaks + MLF10: extended all pads.
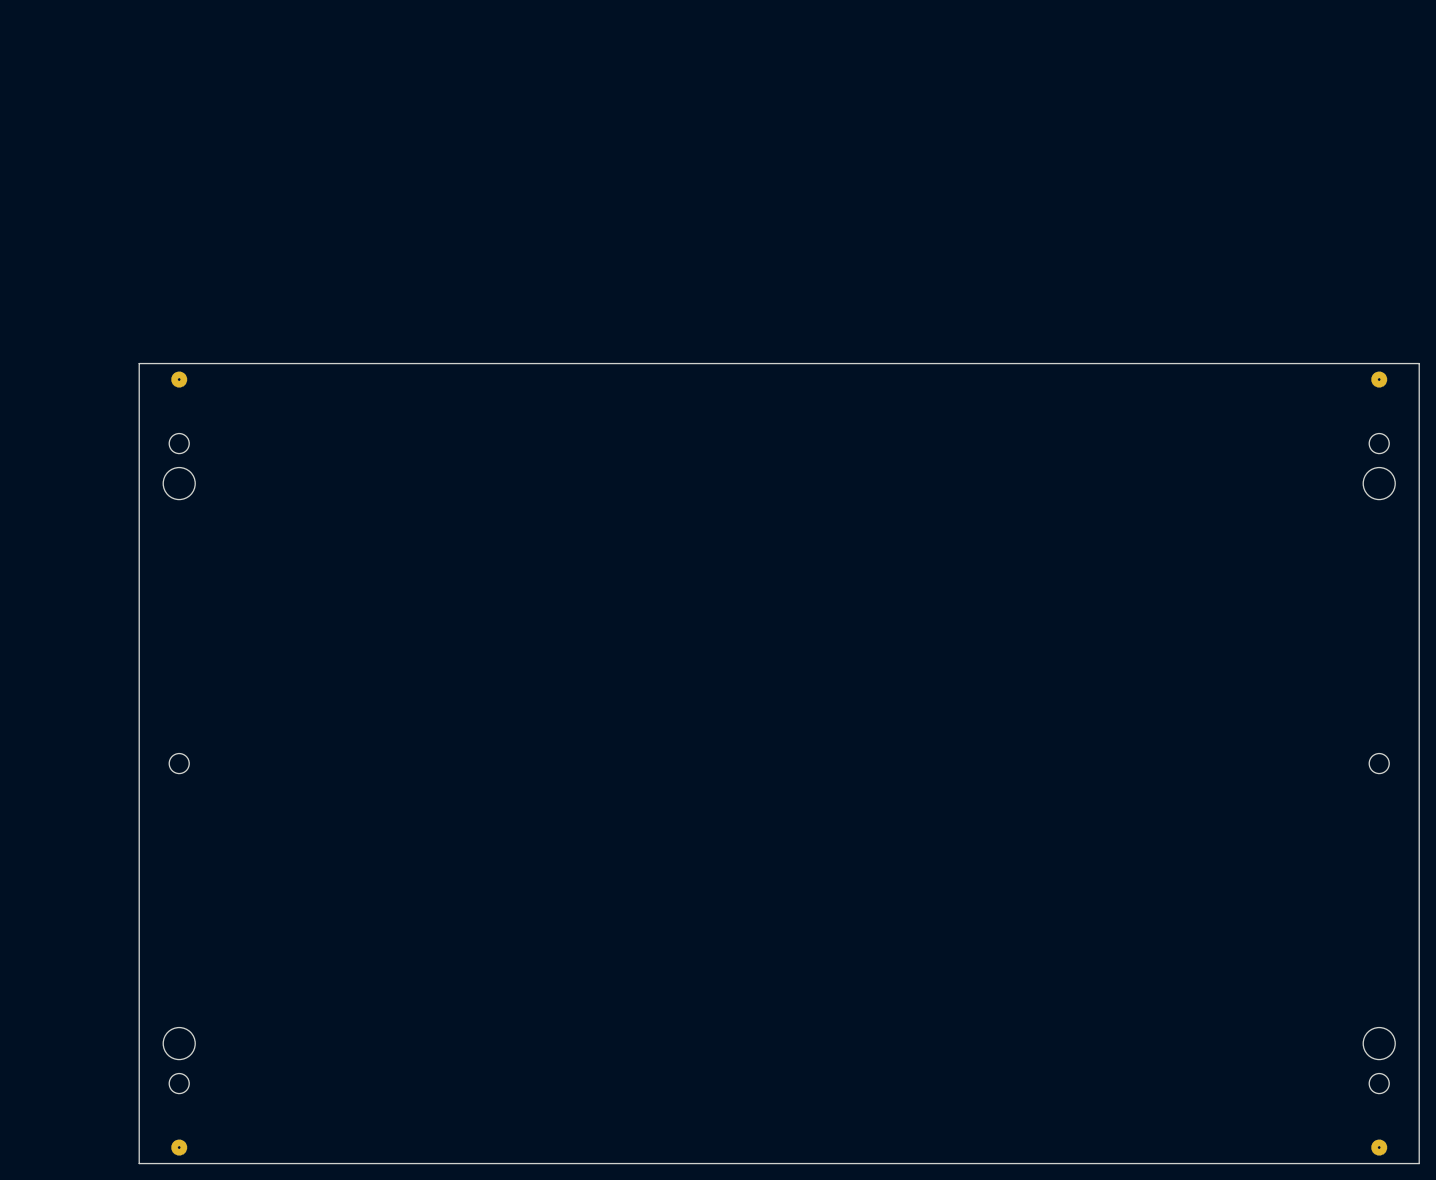
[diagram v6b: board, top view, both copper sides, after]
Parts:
- removed C1 (x4), C2 (x4): 100nF, MADW__C0805
- removed C3 (x4): 4.7µF, MADW__C0805
- removed G1 (x4): OSHW-logo_silkscreen_3mm, OSHW-logo_silkscreen_3mm
- removed G2 (x4): LED_smile_silkscreen_3mm, LED_smile_silkscreen_3mm
- removed IC1 (x4): ATTINY13A-MM, MADW__MLF10
- removed JP1 (x4): ISP, MADW__PIN_ARRAY_3x2_1.27mm
- removed NJ1 (x4): NET-JOIN, MADW__SMD-net-noin-0.5mm
- removed P1 (x4), P2 (x4): CONN_2, MADW__SIL-2
- removed R1 (x4): 100k, MADW__R0603_2
- removed R2 (x4): 150R, MADW__R0603_2
- removed RV1 (x4), RV2 (x4): 50k, MADW__TC33X-POT
- removed T1 (x4): AO3400, MADW__SOT23
- removed U1 (x4): MCP1804-SOT23-5, MADW__SOT23-5
- moved 1PIN 1.00 mm to (105.0, 180.0)
- moved 1PIN 1.00 mm to (105.0, 84.0)
- moved 1PIN 1.00 mm to (255.0, 84.0)
- moved 1PIN 1.00 mm to (255.0, 180.0)
- moved BH1 1.00 mm to (105.0, 97.0)
- moved BH2 1.00 mm to (105.0, 167.0)
- moved BH3 1.00 mm to (255.0, 97.0)
- moved BH4 1.00 mm to (255.0, 167.0)
- moved SM1 1.00 mm to (105.0, 92.0)
- moved SM2 1.00 mm to (105.0, 132.0)
- moved SM3 1.00 mm to (105.0, 172.0)
- moved SM4 1.00 mm to (255.0, 92.0)
- moved SM5 1.00 mm to (255.0, 132.0)
- moved SM6 1.00 mm to (255.0, 172.0)
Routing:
- net GNDPWR: track 164.3 -> 0.00 mm, vias 20 -> 0
- net /Vin: track 149.4 -> 0.00 mm, vias 4 -> 0
- net GND: track 136.6 -> 0.00 mm, vias 8 -> 0
- net /MOSI: track 116.7 -> 0.00 mm
- net VCC: track 79.9 -> 0.00 mm, vias 8 -> 0
- net /POT1: track 51.6 -> 0.00 mm
- net /SCK: track 47.1 -> 0.00 mm
- net /MISO: track 34.6 -> 0.00 mm
- net /POT2: track 34.1 -> 0.00 mm
- net /RESET: track 22.7 -> 0.00 mm
- net /drain: track 14.5 -> 0.00 mm
- net N-000004: track 11.0 -> 0.00 mm
- removed copper zone on F.Cu, net GND
- removed copper zone on B.Cu, net GNDPWR
- removed copper zone on F.Cu, net GNDPWR
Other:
- board text removed: "+"
- board text removed: "-"
- board text removed: "12V"
- board text removed: "2013 - blog.spitzenpfeil.org"
- board text removed: "LED"
- board text removed: "V0.11 POT PWM controller"
